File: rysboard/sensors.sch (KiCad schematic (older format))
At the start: 9 parts, among them J10 ToF3, J11 ToF4, J12 ToF5, J13 ToF6, J14 SPI, J15 Temp, J16 IMU, J8 ToF1, J9 ToF2

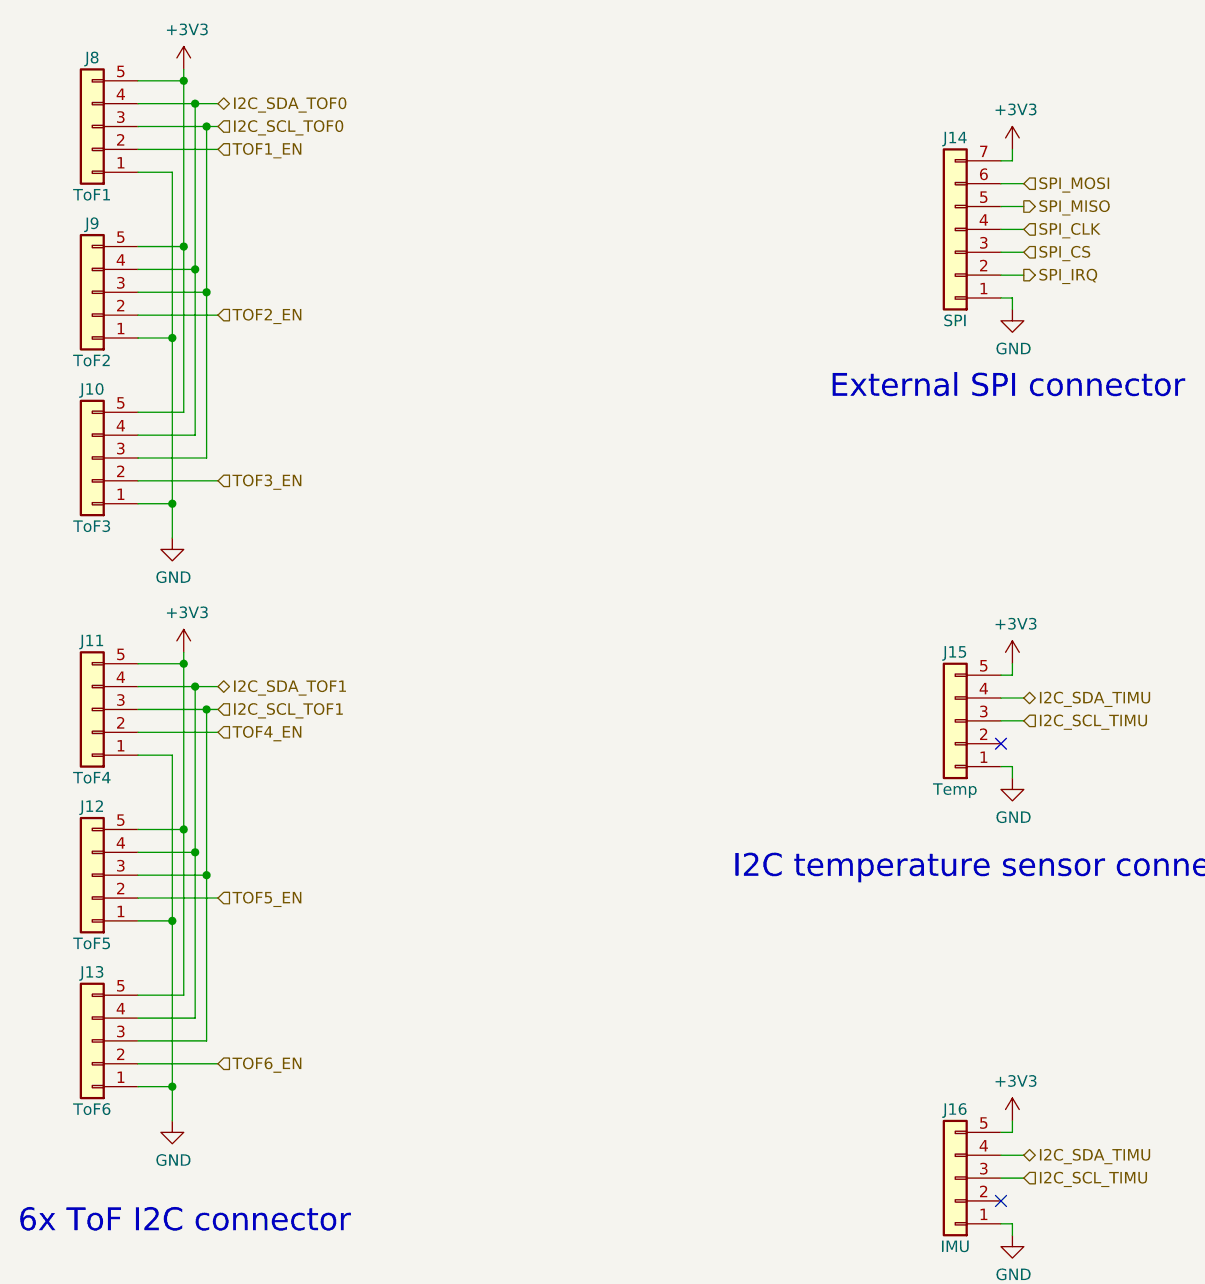
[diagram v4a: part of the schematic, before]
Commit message: rysboard: changed LED and sensors' VCC to 5V
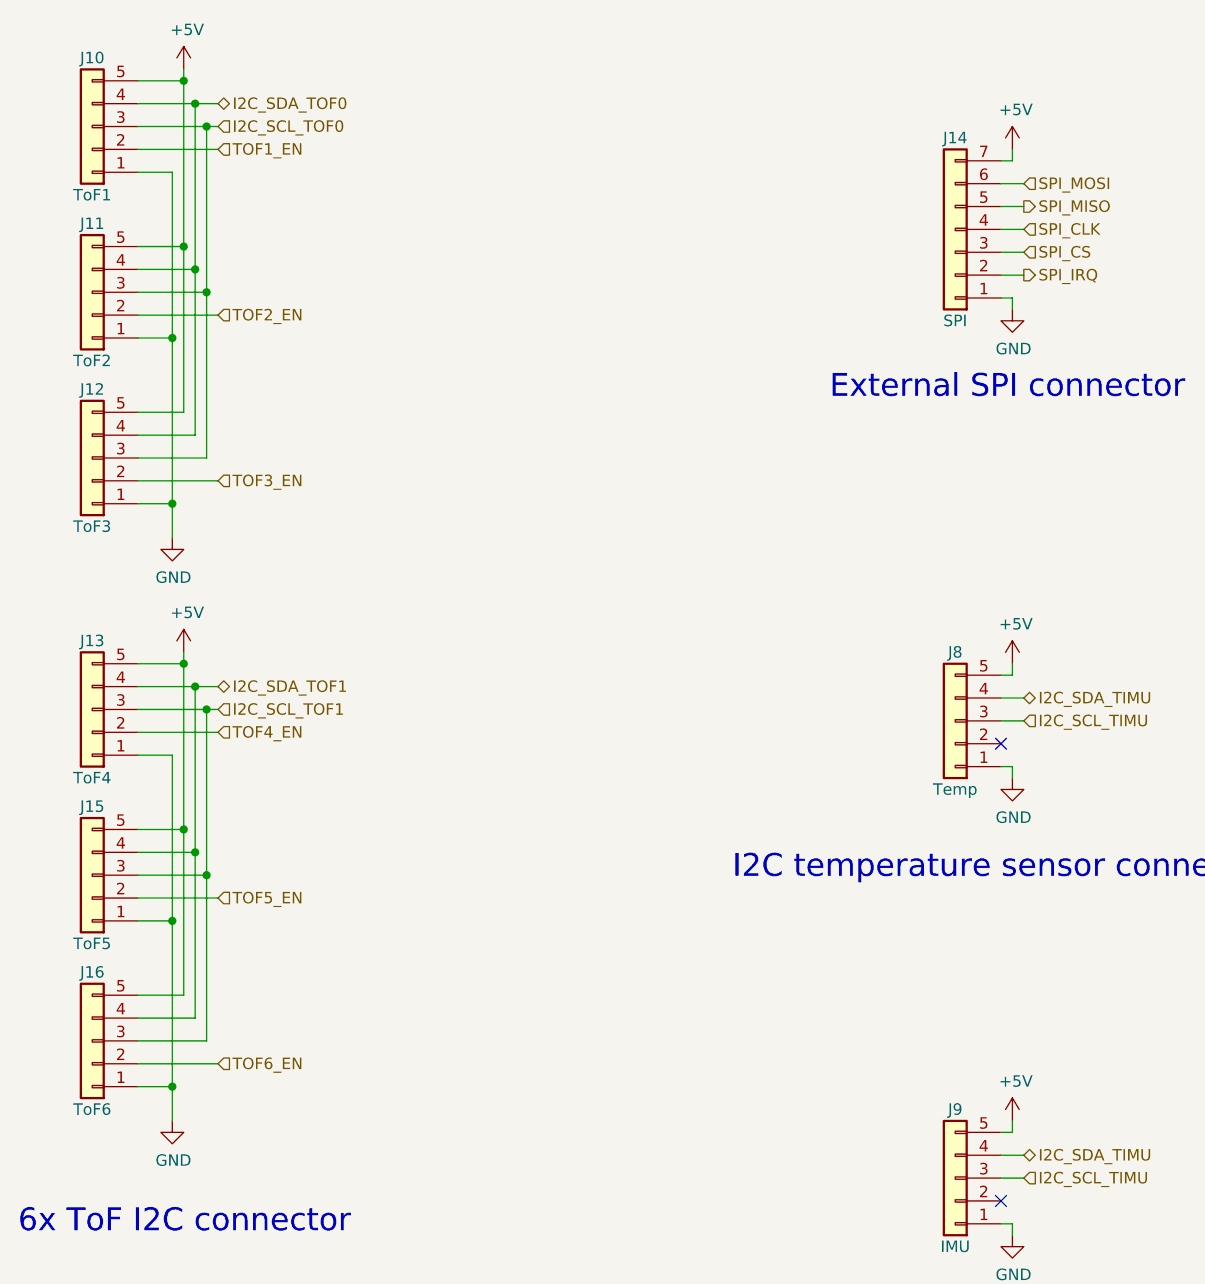
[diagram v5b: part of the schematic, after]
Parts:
- renumbered J8 to J10, J9 to J11, J10 to J12, J11 to J13, J12 to J15, J13 to J16, J15 to J8, J16 to J9
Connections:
- net +3V3 renamed +5V
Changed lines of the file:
@@
 6x ToF I2C connector
 $Comp
-L Connector_Generic:Conn_01x05 J8
+L Connector_Generic:Conn_01x05 J10
 U 1 1 5EB6D871
 P 1775 1400
-F 0 "J8" H 1775 1100 50  0000 C CNN
+F 0 "J10" H 1775 1100 50  0000 C CNN
 F 1 "ToF1" H 1775 1700 50  0000 C CNN
 F 2 "Connector_Molex:Molex_PicoBlade_53047-0510_1x05_P1.25mm_Vertical" H 1775 1400 50  0001 C CNN
@@
 	2175 1200 2175 1150
 $Comp
-L power:+3V3 #PWR024
-U 1 1 5ED4B7A8
-P 2175 1150
-F 0 "#PWR024" H 2175 1000 50  0001 C CNN
-F 1 "+3V3" H 2190 1323 50  0000 C CNN
-F 2 "" H 2175 1150 50  0001 C CNN
-F 3 "" H 2175 1150 50  0001 C CNN
-	1    2175 1150
-	1    0    0    -1
-$EndComp
-$Comp
-L Connector_Generic:Conn_01x05 J9
+L Connector_Generic:Conn_01x05 J11
 U 1 1 5ED64AFD
 P 1775 2125
-F 0 "J9" H 1775 1825 50  0000 C CNN
+F 0 "J11" H 1775 1825 50  0000 C CNN
 F 1 "ToF2" H 1775 2425 50  0000 C CNN
 F 2 "Connector_Molex:Molex_PicoBlade_53047-0510_1x05_P1.25mm_Vertical" H 1775 2125 50  0001 C CNN
@@
 	1975 1925 2175 1925
 $Comp
-L Connector_Generic:Conn_01x05 J10
+L Connector_Generic:Conn_01x05 J12
 U 1 1 5ED67D31
 P 1775 2850
-F 0 "J10" H 1775 2550 50  0000 C CNN
+F 0 "J12" H 1775 2550 50  0000 C CNN
 F 1 "ToF3" H 1775 3150 50  0000 C CNN
 F 2 "Connector_Molex:Molex_PicoBlade_53047-0510_1x05_P1.25mm_Vertical" H 1775 2850 50  0001 C CNN
@@
 	1975 2650 2175 2650
 $Comp
-L Connector_Generic:Conn_01x05 J11
+L Connector_Generic:Conn_01x05 J13
 U 1 1 5ED92371
 P 1775 3950
-F 0 "J11" H 1775 3650 50  0000 C CNN
+F 0 "J13" H 1775 3650 50  0000 C CNN
 F 1 "ToF4" H 1775 4250 50  0000 C CNN
 F 2 "Connector_Molex:Molex_PicoBlade_53047-0510_1x05_P1.25mm_Vertical" H 1775 3950 50  0001 C CNN
@@
 	1975 3750 2175 3750
 $Comp
-L Connector_Generic:Conn_01x05 J12
+L Connector_Generic:Conn_01x05 J15
 U 1 1 5ED92385
 P 1775 4675
-F 0 "J12" H 1775 4375 50  0000 C CNN
+F 0 "J15" H 1775 4375 50  0000 C CNN
 F 1 "ToF5" H 1775 4975 50  0000 C CNN
 F 2 "Connector_Molex:Molex_PicoBlade_53047-0510_1x05_P1.25mm_Vertical" H 1775 4675 50  0001 C CNN
@@
 	1975 4475 2175 4475
 $Comp
-L Connector_Generic:Conn_01x05 J13
+L Connector_Generic:Conn_01x05 J16
 U 1 1 5ED92399
 P 1775 5400
-F 0 "J13" H 1775 5100 50  0000 C CNN
+F 0 "J16" H 1775 5100 50  0000 C CNN
 F 1 "ToF6" H 1775 5700 50  0000 C CNN
 F 2 "Connector_Molex:Molex_PicoBlade_53047-0510_1x05_P1.25mm_Vertical" H 1775 5400 50  0001 C CNN
@@
 	1    5550 1850
 	-1   0    0    1
-$EndComp
-$Comp
-L power:+3V3 #PWR025
-U 1 1 5EE65D43
-P 5800 1500
-F 0 "#PWR025" H 5800 1350 50  0001 C CNN
-F 1 "+3V3" H 5815 1673 50  0000 C CNN
-F 2 "" H 5800 1500 50  0001 C CNN
-F 3 "" H 5800 1500 50  0001 C CNN
-	1    5800 1500
-	1    0    0    -1
 $EndComp
 $Comp
@@
 SPI_IRQ
 $Comp
-L Connector_Generic:Conn_01x05 J15
+L Connector_Generic:Conn_01x05 J8
 U 1 1 5EE7DCB5
 P 5550 4000
-F 0 "J15" H 5550 3700 50  0000 C CNN
+F 0 "J8" H 5550 3700 50  0000 C CNN
 F 1 "Temp" H 5550 4300 50  0000 C CNN
 F 2 "Connector_Molex:Molex_PicoBlade_53047-0510_1x05_P1.25mm_Vertical" H 5550 4000 50  0001 C CNN
@@
 Text HLabel 5850 3900 2    50   BiDi ~ 0
 I2C_SDA_TIMU
-$Comp
-L power:+3V3 #PWR027
-U 1 1 5EE81C29
-P 5800 3750
-F 0 "#PWR027" H 5800 3600 50  0001 C CNN
-F 1 "+3V3" H 5815 3923 50  0000 C CNN
-F 2 "" H 5800 3750 50  0001 C CNN
-F 3 "" H 5800 3750 50  0001 C CNN
-	1    5800 3750
-	1    0    0    -1
-$EndComp
 Wire Wire Line
 	5750 3800 5800 3800
@@
 I2C IMU connector
 $Comp
-L Connector_Generic:Conn_01x05 J16
+L Connector_Generic:Conn_01x05 J9
 U 1 1 5EE95D68
 P 5550 6000
-F 0 "J16" H 5550 5700 50  0000 C CNN
+F 0 "J9" H 5550 5700 50  0000 C CNN
 F 1 "IMU" H 5550 6300 50  0000 C CNN
 F 2 "Connector_Molex:Molex_PicoBlade_53047-0510_1x05_P1.25mm_Vertical" H 5550 6000 50  0001 C CNN
@@
 Text HLabel 5850 5900 2    50   BiDi ~ 0
 I2C_SDA_TIMU
-$Comp
-L power:+3V3 #PWR029
-U 1 1 5EE95D70
-P 5800 5750
-F 0 "#PWR029" H 5800 5600 50  0001 C CNN
-F 1 "+3V3" H 5815 5923 50  0000 C CNN
-F 2 "" H 5800 5750 50  0001 C CNN
-F 3 "" H 5800 5750 50  0001 C CNN
-	1    5800 5750
-	1    0    0    -1
-$EndComp
 Wire Wire Line
 	5750 5800 5800 5800
@@
 Text HLabel 2325 3850 2    50   BiDi ~ 0
 I2C_SDA_TOF1
-$Comp
-L power:+3V3 #PWR0109
-U 1 1 5E9EC114
-P 2175 3700
-F 0 "#PWR0109" H 2175 3550 50  0001 C CNN
-F 1 "+3V3" H 2190 3873 50  0000 C CNN
-F 2 "" H 2175 3700 50  0001 C CNN
-F 3 "" H 2175 3700 50  0001 C CNN
-	1    2175 3700
-	1    0    0    -1
-$EndComp
 Wire Wire Line
 	2175 3750 2175 3700
@@
 $EndComp
 Connection ~ 2125 3050
+$Comp
+L power:+5V #PWR0102
+U 1 1 5ECB6D85
+P 2175 1150
+F 0 "#PWR0102" H 2175 1000 50  0001 C CNN
+F 1 "+5V" H 2190 1323 50  0000 C CNN
+F 2 "" H 2175 1150 50  0001 C CNN
+F 3 "" H 2175 1150 50  0001 C CNN
+	1    2175 1150
+	1    0    0    -1
+$EndComp
+$Comp
+L power:+5V #PWR0104
+U 1 1 5ECB8673
+P 2175 3700
+F 0 "#PWR0104" H 2175 3550 50  0001 C CNN
+F 1 "+5V" H 2190 3873 50  0000 C CNN
+F 2 "" H 2175 3700 50  0001 C CNN
+F 3 "" H 2175 3700 50  0001 C CNN
+	1    2175 3700
+	1    0    0    -1
+$EndComp
+$Comp
+L power:+5V #PWR0109
+U 1 1 5ECB9E16
+P 5800 3750
+F 0 "#PWR0109" H 5800 3600 50  0001 C CNN
+F 1 "+5V" H 5815 3923 50  0000 C CNN
+F 2 "" H 5800 3750 50  0001 C CNN
+F 3 "" H 5800 3750 50  0001 C CNN
+	1    5800 3750
+	1    0    0    -1
+$EndComp
+$Comp
+L power:+5V #PWR0111
+U 1 1 5ECBB5E8
+P 5800 1500
+F 0 "#PWR0111" H 5800 1350 50  0001 C CNN
+F 1 "+5V" H 5815 1673 50  0000 C CNN
+F 2 "" H 5800 1500 50  0001 C CNN
+F 3 "" H 5800 1500 50  0001 C CNN
+	1    5800 1500
+	1    0    0    -1
+$EndComp
+$Comp
+L power:+5V #PWR0112
+U 1 1 5ECBCED2
+P 5800 5750
+F 0 "#PWR0112" H 5800 5600 50  0001 C CNN
+F 1 "+5V" H 5815 5923 50  0000 C CNN
+F 2 "" H 5800 5750 50  0001 C CNN
+F 3 "" H 5800 5750 50  0001 C CNN
+	1    5800 5750
+	1    0    0    -1
+$EndComp
 $EndSCHEMATC

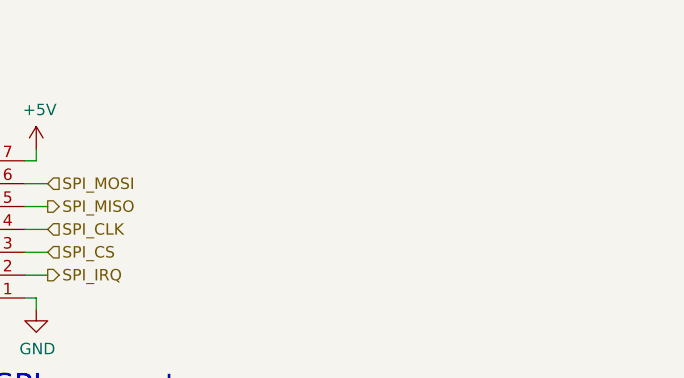
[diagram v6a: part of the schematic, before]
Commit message: rysboard: move D8 before converter feedback; replace U5 with counterpart of higher availability; fix U4 wiring; improve GND connections to motor drivers
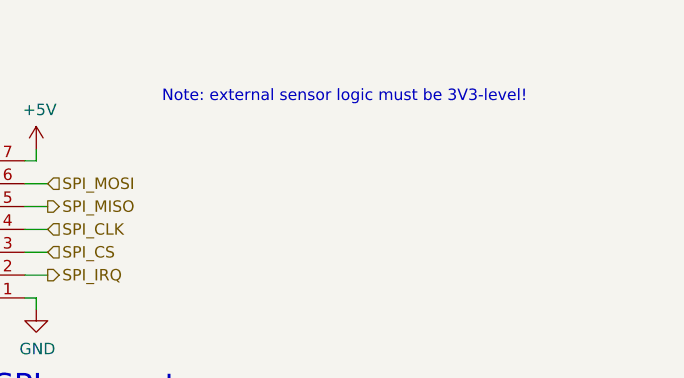
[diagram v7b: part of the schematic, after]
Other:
- note added: "Note: external sensor logic must be 3V3-level!"
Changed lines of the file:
@@
 	1    0    0    -1
 $EndComp
+Text Notes 6350 1300 0    50   ~ 0
+Note: external sensor logic must be 3V3-level!
 $EndSCHEMATC

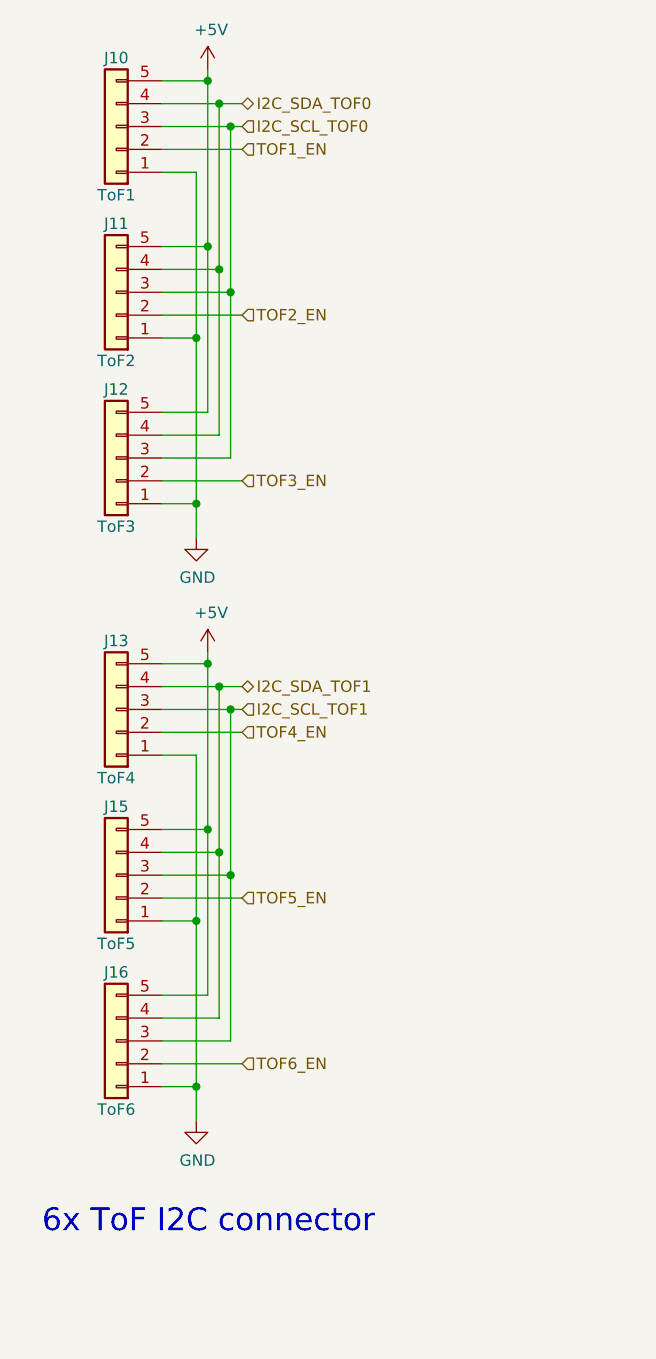
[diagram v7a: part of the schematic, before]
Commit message: added Battery Baalancing, Reverse polarity protection circuits and skeleton of power managment
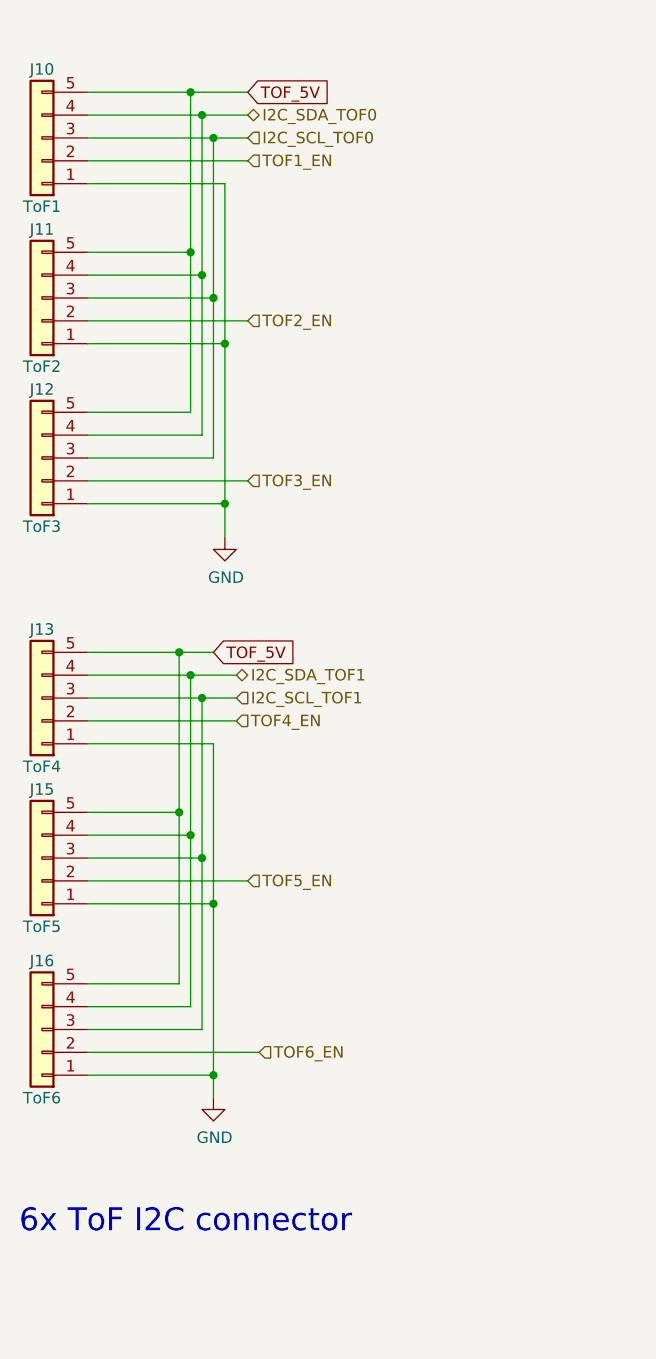
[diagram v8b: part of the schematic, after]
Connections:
- net +5V: no longer J10.5 (Pin_5), J11.5 (Pin_5), J12.5 (Pin_5), J13.5 (Pin_5), J15.5 (Pin_5), J16.5 (Pin_5)
- new net TOF_5V: J10.5 (Pin_5), J11.5 (Pin_5), J12.5 (Pin_5), J13.5 (Pin_5), J15.5 (Pin_5), J16.5 (Pin_5)
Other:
- moved on the sheet: J10, J11, J12, J13, J15, J16
